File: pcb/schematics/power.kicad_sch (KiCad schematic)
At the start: 7 parts

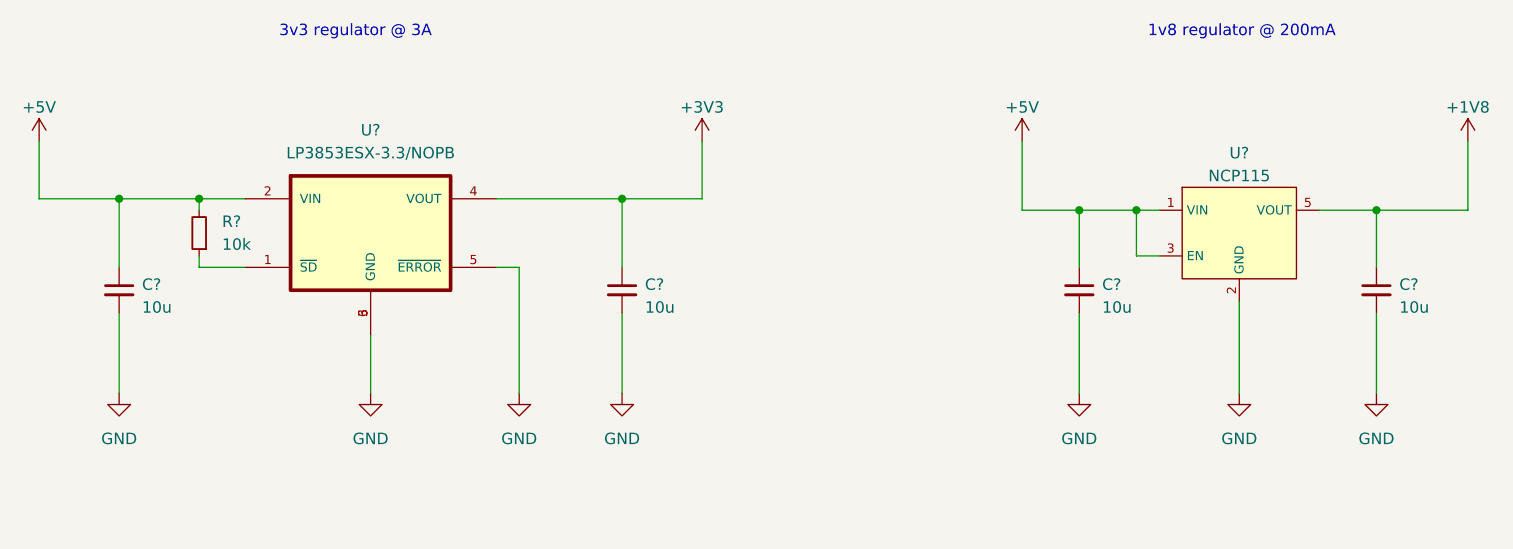
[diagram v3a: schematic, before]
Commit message: choose components and add footprints
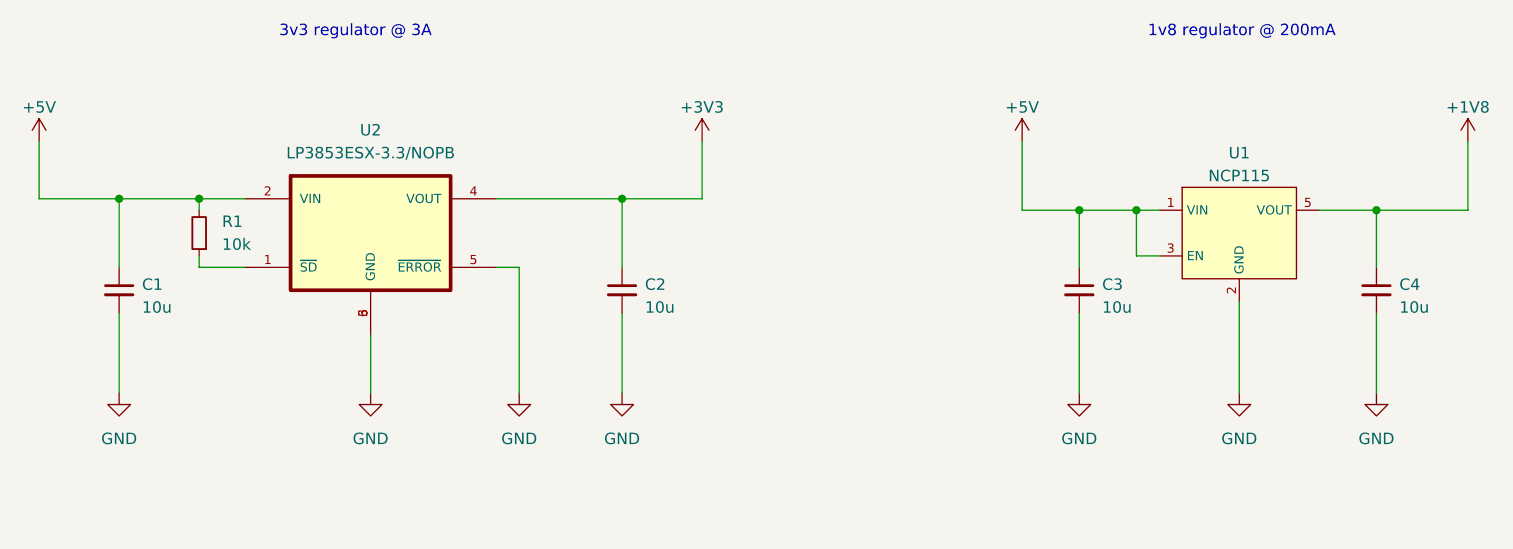
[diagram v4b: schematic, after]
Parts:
- C1, C2, C3, C4: renamed from C?; footprint (none) -> Capacitor_SMD:C_0805_2012Metric; Part Number (none) -> JMK212ABJ106MG-T
- R1: renamed from R?; footprint (none) -> Resistor_SMD:R_0603_1608Metric; Part Number (none) -> RC0603JR-0710KL
- U1: renamed from U?; footprint Package_DFN_QFN:OnSemi_XDFN4-1EP_1.0x1.0mm_EP0.52x0.52mm -> NCP115ASN180T2G:NCP115ASN180T2G; Part Number (none) -> NCP115ASN180T2G
- U2: renamed from U?; footprint VREG_TPS79625KTTR -> LP3853ESX-3_3:LP3853ESX-3_3; Part Number (none) -> LP3853ESX-3.3/NOPB
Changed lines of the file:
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@@
   (symbol (lib_id "power:GND") (at 72.39 96.52 0) (unit 1)
     (in_bom yes) (on_board yes) (fields_autoplaced)
-    (property "Reference" "#PWR?" (id 0) (at 72.39 102.87 0)
+    (property "Reference" "#PWR05" (id 0) (at 72.39 102.87 0)
       (effects (font (size 1.27 1.27)) hide)
     )
@@
   (symbol (lib_id "Device:C_Small") (at 212.09 85.09 0) (unit 1)
     (in_bom yes) (on_board yes) (fields_autoplaced)
-    (property "Reference" "C?" (id 0) (at 214.63 84.4613 0)
+    (property "Reference" "C4" (id 0) (at 214.63 84.4613 0)
       (effects (font (size 1.27 1.27)) (justify left))
     )
@@
       (effects (font (size 1.27 1.27)) (justify left))
     )
-    (property "Footprint" "" (id 2) (at 212.09 85.09 0)
+    (property "Footprint" "Capacitor_SMD:C_0805_2012Metric" (id 2) (at 212.09 85.09 0)
       (effects (font (size 1.27 1.27)) hide)
     )
@@
       (effects (font (size 1.27 1.27)) hide)
     )
+    (property "Part Number" "JMK212ABJ106MG-T" (id 4) (at 212.09 85.09 0)
+      (effects (font (size 1.27 1.27)) hide)
+    )
     (pin "1")
     (pin "2")
@@
   (symbol (lib_id "NCP115:NCP115") (at 196.85 78.74 0) (unit 1)
     (in_bom yes) (on_board yes) (fields_autoplaced)
-    (property "Reference" "U?" (id 0) (at 196.85 69.85 0)
+    (property "Reference" "U1" (id 0) (at 196.85 69.85 0)
       (effects (font (size 1.27 1.27)))
     )
@@
       (effects (font (size 1.27 1.27)))
     )
-    (property "Footprint" "Package_DFN_QFN:OnSemi_XDFN4-1EP_1.0x1.0mm_EP0.52x0.52mm" (id 2) (at 196.85 71.12 0)
+    (property "Footprint" "NCP115ASN180T2G:NCP115ASN180T2G" (id 2) (at 196.85 71.12 0)
       (effects (font (size 1.27 1.27)) hide)
     )
     (property "Datasheet" "" (id 3) (at 196.85 71.12 0)
+      (effects (font (size 1.27 1.27)) hide)
+    )
+    (property "Part Number" "NCP115ASN180T2G" (id 4) (at 196.85 78.74 0)
       (effects (font (size 1.27 1.27)) hide)
     )
@@
   (symbol (lib_id "power:+5V") (at 63.5 68.58 0) (unit 1)
     (in_bom yes) (on_board yes) (fields_autoplaced)
-    (property "Reference" "#PWR?" (id 0) (at 63.5 72.39 0)
+    (property "Reference" "#PWR01" (id 0) (at 63.5 72.39 0)
       (effects (font (size 1.27 1.27)) hide)
     )
@@
   (symbol (lib_id "power:GND") (at 212.09 96.52 0) (unit 1)
     (in_bom yes) (on_board yes) (fields_autoplaced)
-    (property "Reference" "#PWR?" (id 0) (at 212.09 102.87 0)
+    (property "Reference" "#PWR011" (id 0) (at 212.09 102.87 0)
       (effects (font (size 1.27 1.27)) hide)
     )
@@
   (symbol (lib_id "Device:C_Small") (at 179.07 85.09 0) (unit 1)
     (in_bom yes) (on_board yes) (fields_autoplaced)
-    (property "Reference" "C?" (id 0) (at 181.61 84.4613 0)
+    (property "Reference" "C3" (id 0) (at 181.61 84.4613 0)
       (effects (font (size 1.27 1.27)) (justify left))
     )
@@
       (effects (font (size 1.27 1.27)) (justify left))
     )
-    (property "Footprint" "" (id 2) (at 179.07 85.09 0)
+    (property "Footprint" "Capacitor_SMD:C_0805_2012Metric" (id 2) (at 179.07 85.09 0)
       (effects (font (size 1.27 1.27)) hide)
     )
@@
       (effects (font (size 1.27 1.27)) hide)
     )
+    (property "Part Number" "JMK212ABJ106MG-T" (id 4) (at 179.07 85.09 0)
+      (effects (font (size 1.27 1.27)) hide)
+    )
     (pin "1")
     (pin "2")
@@
   (symbol (lib_id "power:GND") (at 179.07 96.52 0) (unit 1)
     (in_bom yes) (on_board yes) (fields_autoplaced)
-    (property "Reference" "#PWR?" (id 0) (at 179.07 102.87 0)
+    (property "Reference" "#PWR09" (id 0) (at 179.07 102.87 0)
       (effects (font (size 1.27 1.27)) hide)
     )
@@
   (symbol (lib_id "power:+5V") (at 172.72 68.58 0) (unit 1)
     (in_bom yes) (on_board yes) (fields_autoplaced)
-    (property "Reference" "#PWR?" (id 0) (at 172.72 72.39 0)
+    (property "Reference" "#PWR03" (id 0) (at 172.72 72.39 0)
       (effects (font (size 1.27 1.27)) hide)
     )
@@
   (symbol (lib_id "power:+3V3") (at 137.16 68.58 0) (unit 1)
     (in_bom yes) (on_board yes) (fields_autoplaced)
-    (property "Reference" "#PWR?" (id 0) (at 137.16 72.39 0)
+    (property "Reference" "#PWR02" (id 0) (at 137.16 72.39 0)
       (effects (font (size 1.27 1.27)) hide)
     )
@@
   (symbol (lib_id "LP3853ESX-3.3_NOPB:LP3853ESX-3.3{slash}NOPB") (at 109.22 82.55 0) (unit 1)
     (in_bom yes) (on_board yes)
-    (property "Reference" "U?" (id 0) (at 100.33 67.31 0)
+    (property "Reference" "U2" (id 0) (at 100.33 67.31 0)
       (effects (font (size 1.27 1.27)))
     )
@@
       (effects (font (size 1.27 1.27)))
     )
-    (property "Footprint" "VREG_TPS79625KTTR" (id 2) (at 109.22 82.55 0)
+    (property "Footprint" "LP3853ESX-3_3:LP3853ESX-3_3" (id 2) (at 109.22 82.55 0)
       (effects (font (size 1.27 1.27)) (justify left bottom) hide)
     )
     (property "Datasheet" "https://www.ti.com/lit/ds/symlink/lp3853.pdf?HQS=dis-mous-null-mousermode-dsf-pf-null-wwe&ts=1634641603473&ref_url=https%253A%252F%252Fcz.mouser.com%252F" (id 3) (at 109.22 82.55 0)
       (effects (font (size 1.27 1.27)) (justify left bottom) hide)
+    )
+    (property "Part Number" "LP3853ESX-3.3/NOPB" (id 4) (at 109.22 82.55 0)
+      (effects (font (size 1.27 1.27)) hide)
     )
     (pin "1")
@@
   (symbol (lib_id "power:GND") (at 116.84 96.52 0) (unit 1)
     (in_bom yes) (on_board yes) (fields_autoplaced)
-    (property "Reference" "#PWR?" (id 0) (at 116.84 102.87 0)
+    (property "Reference" "#PWR07" (id 0) (at 116.84 102.87 0)
       (effects (font (size 1.27 1.27)) hide)
     )
@@
   (symbol (lib_id "Device:C_Small") (at 72.39 85.09 0) (unit 1)
     (in_bom yes) (on_board yes) (fields_autoplaced)
-    (property "Reference" "C?" (id 0) (at 74.93 84.4613 0)
+    (property "Reference" "C1" (id 0) (at 74.93 84.4613 0)
       (effects (font (size 1.27 1.27)) (justify left))
     )
@@
       (effects (font (size 1.27 1.27)) (justify left))
     )
-    (property "Footprint" "" (id 2) (at 72.39 85.09 0)
+    (property "Footprint" "Capacitor_SMD:C_0805_2012Metric" (id 2) (at 72.39 85.09 0)
       (effects (font (size 1.27 1.27)) hide)
     )
@@
       (effects (font (size 1.27 1.27)) hide)
     )
+    (property "Part Number" "JMK212ABJ106MG-T" (id 4) (at 72.39 85.09 0)
+      (effects (font (size 1.27 1.27)) hide)
+    )
     (pin "1")
     (pin "2")
@@
   (symbol (lib_id "power:GND") (at 196.85 96.52 0) (unit 1)
     (in_bom yes) (on_board yes) (fields_autoplaced)
-    (property "Reference" "#PWR?" (id 0) (at 196.85 102.87 0)
+    (property "Reference" "#PWR010" (id 0) (at 196.85 102.87 0)
       (effects (font (size 1.27 1.27)) hide)
     )
@@
   (symbol (lib_id "Device:R_Small") (at 81.28 78.74 180) (unit 1)
     (in_bom yes) (on_board yes)
-    (property "Reference" "R?" (id 0) (at 83.82 77.47 0)
+    (property "Reference" "R1" (id 0) (at 83.82 77.47 0)
       (effects (font (size 1.27 1.27)) (justify right))
     )
@@
       (effects (font (size 1.27 1.27)) (justify right))
     )
-    (property "Footprint" "" (id 2) (at 81.28 78.74 0)
+    (property "Footprint" "Resistor_SMD:R_0603_1608Metric" (id 2) (at 81.28 78.74 0)
       (effects (font (size 1.27 1.27)) hide)
     )
@@
       (effects (font (size 1.27 1.27)) hide)
     )
+    (property "Part Number" "RC0603JR-0710KL" (id 4) (at 81.28 78.74 0)
+      (effects (font (size 1.27 1.27)) hide)
+    )
     (pin "1")
     (pin "2")
@@
   (symbol (lib_id "power:GND") (at 100.33 96.52 0) (unit 1)
     (in_bom yes) (on_board yes) (fields_autoplaced)
-    (property "Reference" "#PWR?" (id 0) (at 100.33 102.87 0)
+    (property "Reference" "#PWR06" (id 0) (at 100.33 102.87 0)
       (effects (font (size 1.27 1.27)) hide)
     )
@@
   (symbol (lib_id "Device:C_Small") (at 128.27 85.09 0) (unit 1)
     (in_bom yes) (on_board yes) (fields_autoplaced)
-    (property "Reference" "C?" (id 0) (at 130.81 84.4613 0)
+    (property "Reference" "C2" (id 0) (at 130.81 84.4613 0)
       (effects (font (size 1.27 1.27)) (justify left))
     )
@@
       (effects (font (size 1.27 1.27)) (justify left))
     )
-    (property "Footprint" "" (id 2) (at 128.27 85.09 0)
+    (property "Footprint" "Capacitor_SMD:C_0805_2012Metric" (id 2) (at 128.27 85.09 0)
       (effects (font (size 1.27 1.27)) hide)
     )
@@
       (effects (font (size 1.27 1.27)) hide)
     )
+    (property "Part Number" "JMK212ABJ106MG-T" (id 4) (at 128.27 85.09 0)
+      (effects (font (size 1.27 1.27)) hide)
+    )
     (pin "1")
     (pin "2")
@@
   (symbol (lib_id "power:+1V8") (at 222.25 68.58 0) (unit 1)
     (in_bom yes) (on_board yes) (fields_autoplaced)
-    (property "Reference" "#PWR?" (id 0) (at 222.25 72.39 0)
+    (property "Reference" "#PWR04" (id 0) (at 222.25 72.39 0)
       (effects (font (size 1.27 1.27)) hide)
     )
@@
   (symbol (lib_id "power:GND") (at 128.27 96.52 0) (unit 1)
     (in_bom yes) (on_board yes) (fields_autoplaced)
-    (property "Reference" "#PWR?" (id 0) (at 128.27 102.87 0)
-      (effects (font (size 1.27 1.27)) hide)
-    )
+    (property "Reference" "#PWR08" (id 0) (at 128.27 102.87 0)
+      (effects (font (size 1.27 1.27)) hide)
+    )

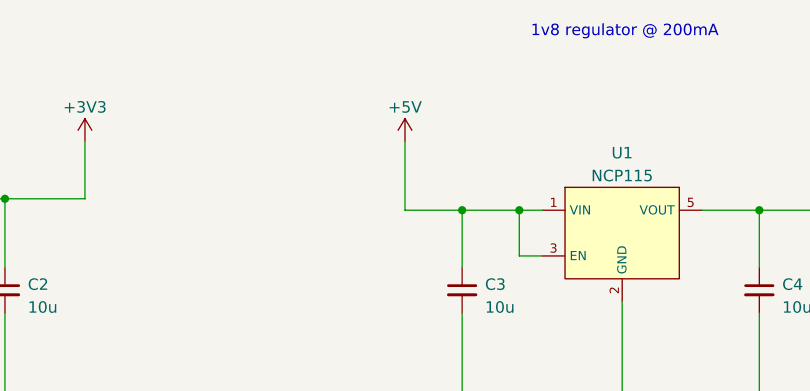
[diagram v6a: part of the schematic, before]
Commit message: add the 3v3 voltage regulator
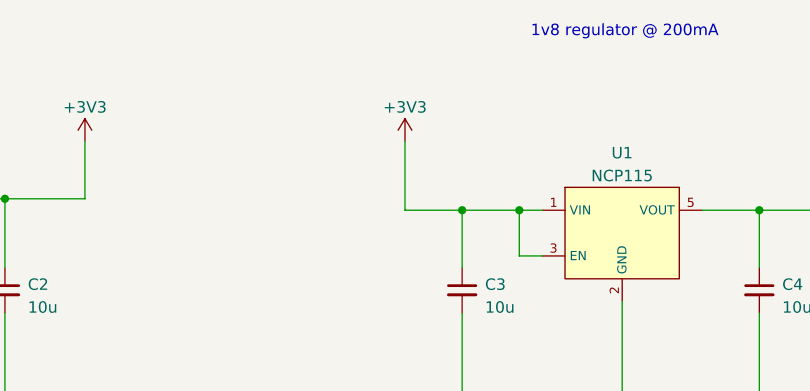
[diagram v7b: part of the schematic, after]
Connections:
- net +3V3: now also C3.1, U1.1 (VIN), U1.3 (EN)
- net +5V: no longer C3.1, U1.1 (VIN), U1.3 (EN)
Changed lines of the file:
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@@
-    (pin "1")
-  )
-  (symbol (lib_id "power:+5V") (at 172.72 68.58 0) (unit 1)
-    (in_bom yes) (on_board yes) (fields_autoplaced)
-    (property "Reference" "#PWR03" (id 0) (at 172.72 72.39 0)
-      (effects (font (size 1.27 1.27)) hide)
-    )
-    (property "Value" "+5V" (id 1) (at 172.72 64.77 0)
-      (effects (font (size 1.27 1.27)))
-    )
-    (property "Footprint" "" (id 2) (at 172.72 68.58 0)
-      (effects (font (size 1.27 1.27)) hide)
-    )
-    (property "Datasheet" "" (id 3) (at 172.72 68.58 0)
-      (effects (font (size 1.27 1.27)) hide)
-    )
     (pin "1")
   )
@@
       (effects (font (size 1.27 1.27)) hide)
     )
+    (pin "1")
+  )
+  (symbol (lib_id "power:+3V3") (at 172.72 68.58 0) (unit 1)
+    (in_bom yes) (on_board yes) (fields_autoplaced)
+    (property "Reference" "#PWR?" (id 0) (at 172.72 72.39 0)
+      (effects (font (size 1.27 1.27)) hide)
+    )
+    (property "Value" "+3V3" (id 1) (at 172.72 64.77 0)
+      (effects (font (size 1.27 1.27)))
+    )
+    (property "Footprint" "" (id 2) (at 172.72 68.58 0)
+      (effects (font (size 1.27 1.27)) hide)
+    )
+    (property "Datasheet" "" (id 3) (at 172.72 68.58 0)
+      (effects (font (size 1.27 1.27)) hide)
+    )
